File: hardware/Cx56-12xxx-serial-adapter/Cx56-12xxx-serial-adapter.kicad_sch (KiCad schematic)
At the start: 14 parts, among them J1 Conn_01x05_Pin, U1 74HC595, U2 74HC595, U3 CC56-12EWA

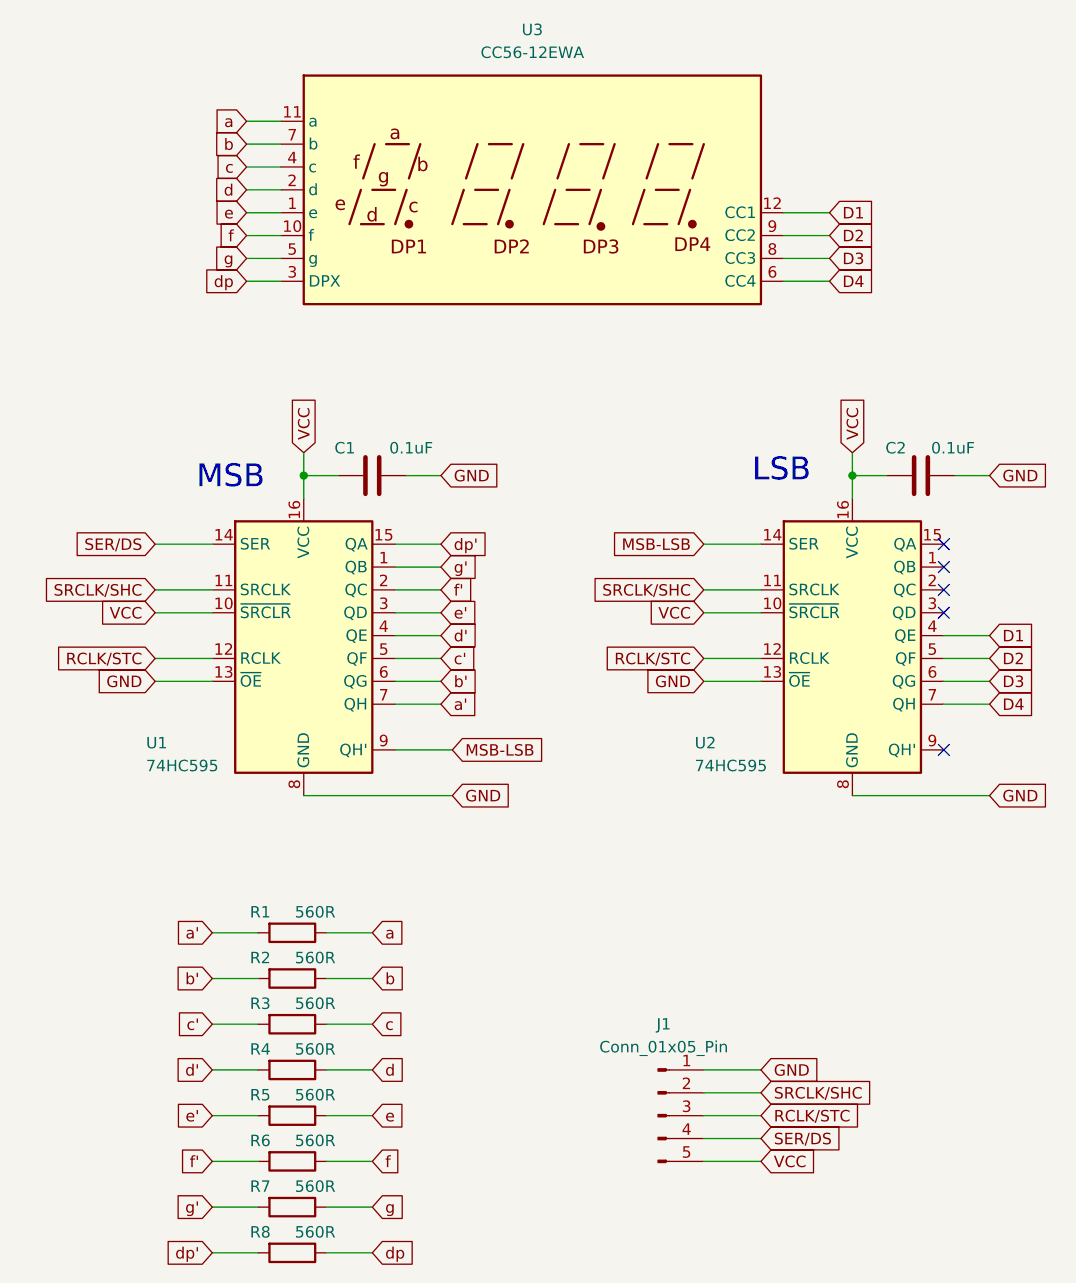
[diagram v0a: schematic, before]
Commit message: 002: from MSB to LSB shift register data transmission
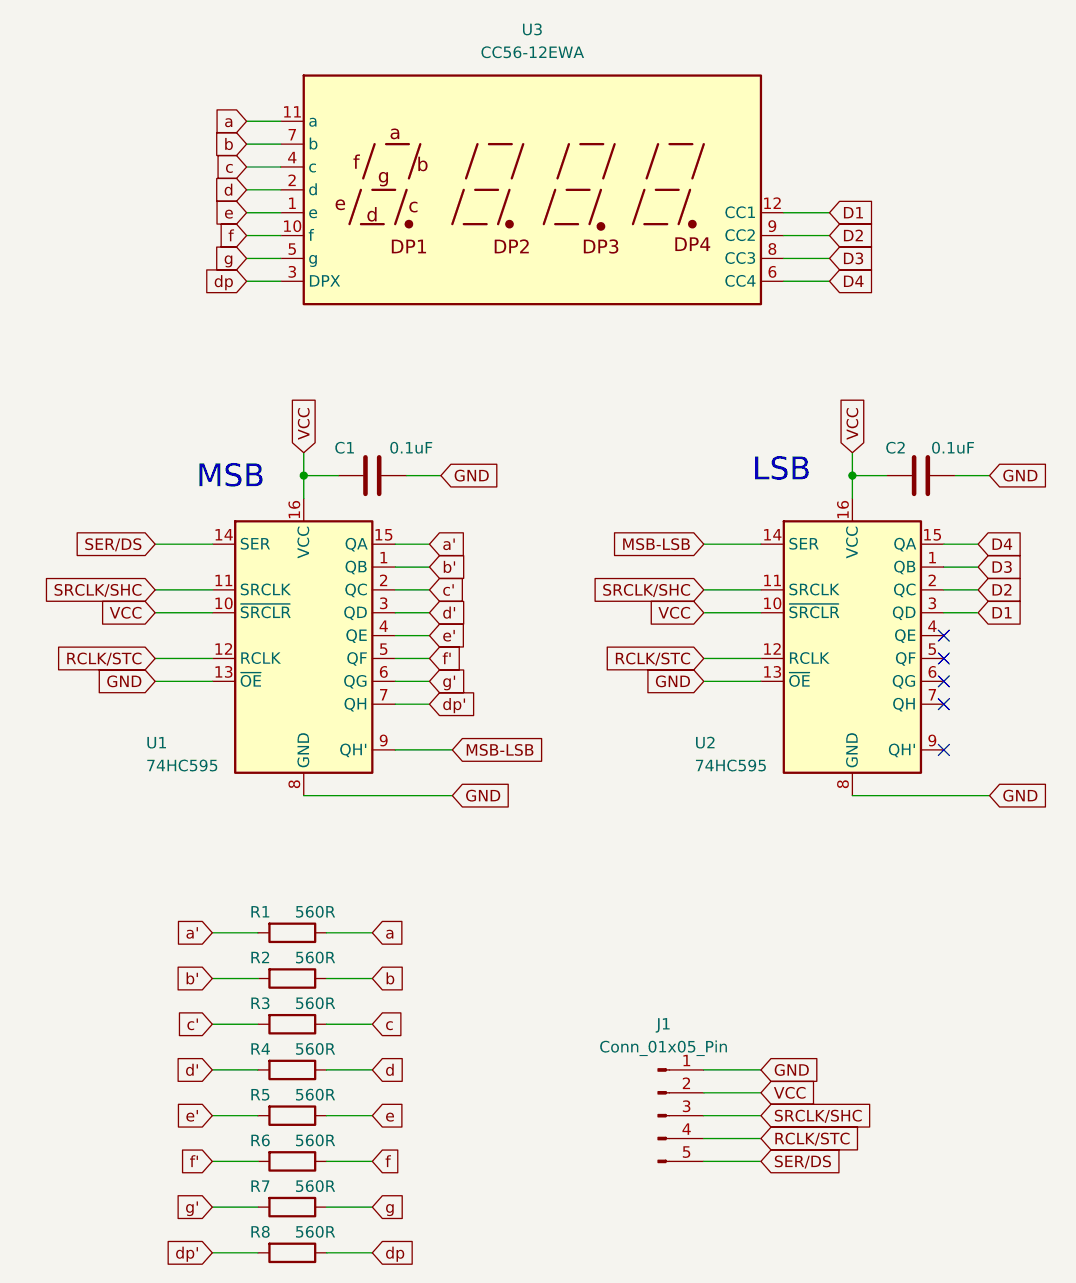
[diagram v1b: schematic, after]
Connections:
- net D1: now also U2.3 (QD); no longer U2.4 (QE)
- net D2: now also U2.2 (QC); no longer U2.5 (QF)
- net D3: now also U2.1 (QB); no longer U2.6 (QG)
- net D4: now also U2.15 (QA); no longer U2.7 (QH)
- net RCLK/STC: now also J1.4 (Pin_4); no longer J1.3 (Pin_3)
- net SER/DS: now also J1.5 (Pin_5); no longer J1.4 (Pin_4)
- net SRCLK/SHC: now also J1.3 (Pin_3); no longer J1.2 (Pin_2)
- net VCC: now also J1.2 (Pin_2); no longer J1.5 (Pin_5)
- net a': now also U1.15 (QA); no longer U1.7 (QH)
- net b': now also U1.1 (QB); no longer U1.6 (QG)
- net c': now also U1.2 (QC); no longer U1.5 (QF)
- net d': now also U1.3 (QD); no longer U1.4 (QE)
- net dp': now also U1.7 (QH); no longer U1.15 (QA)
- net e': now also U1.4 (QE); no longer U1.3 (QD)
- net f': now also U1.5 (QF); no longer U1.2 (QC)
- net g': now also U1.6 (QG); no longer U1.1 (QB)
